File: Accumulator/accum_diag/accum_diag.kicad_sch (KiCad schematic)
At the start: 20 parts, among them K1 Contactor, K2 Contactor, K3 Precharge Relay, U2 Precharge

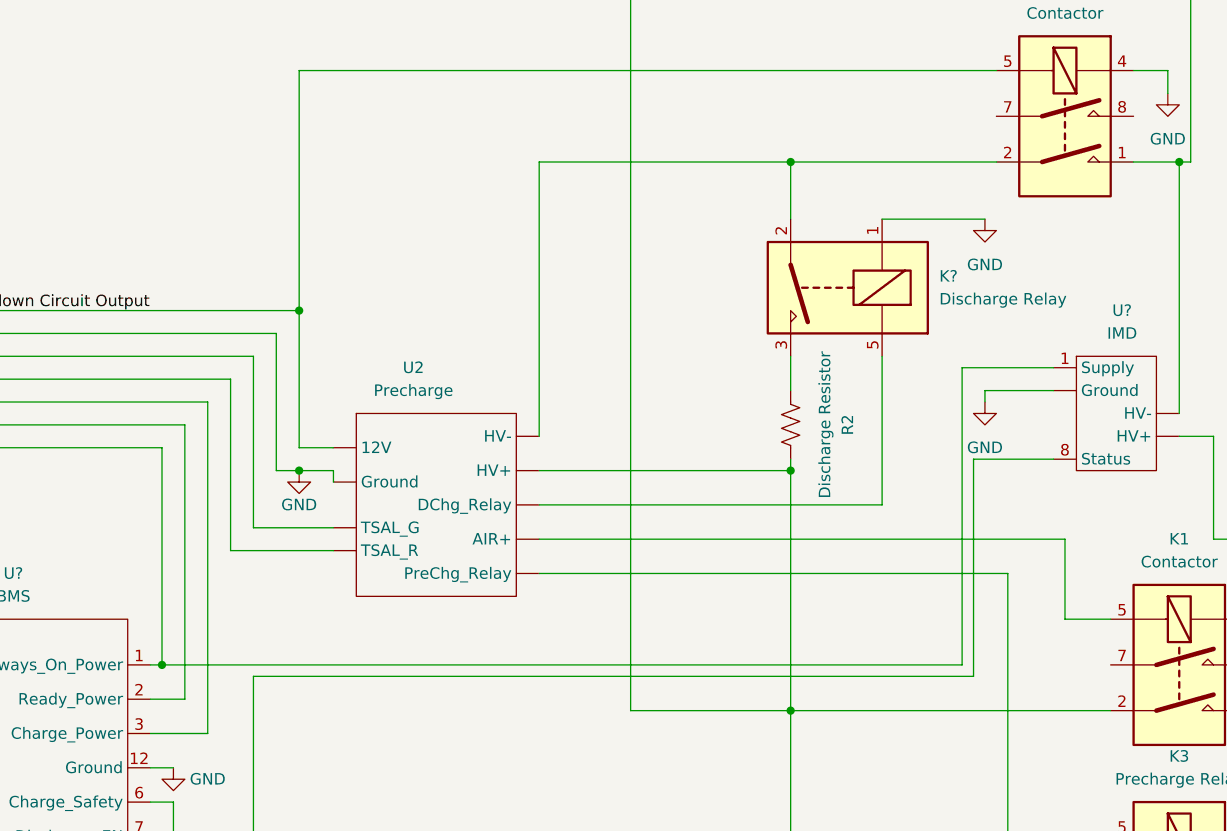
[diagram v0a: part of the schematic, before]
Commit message: Added GLV connection to precharge symbol
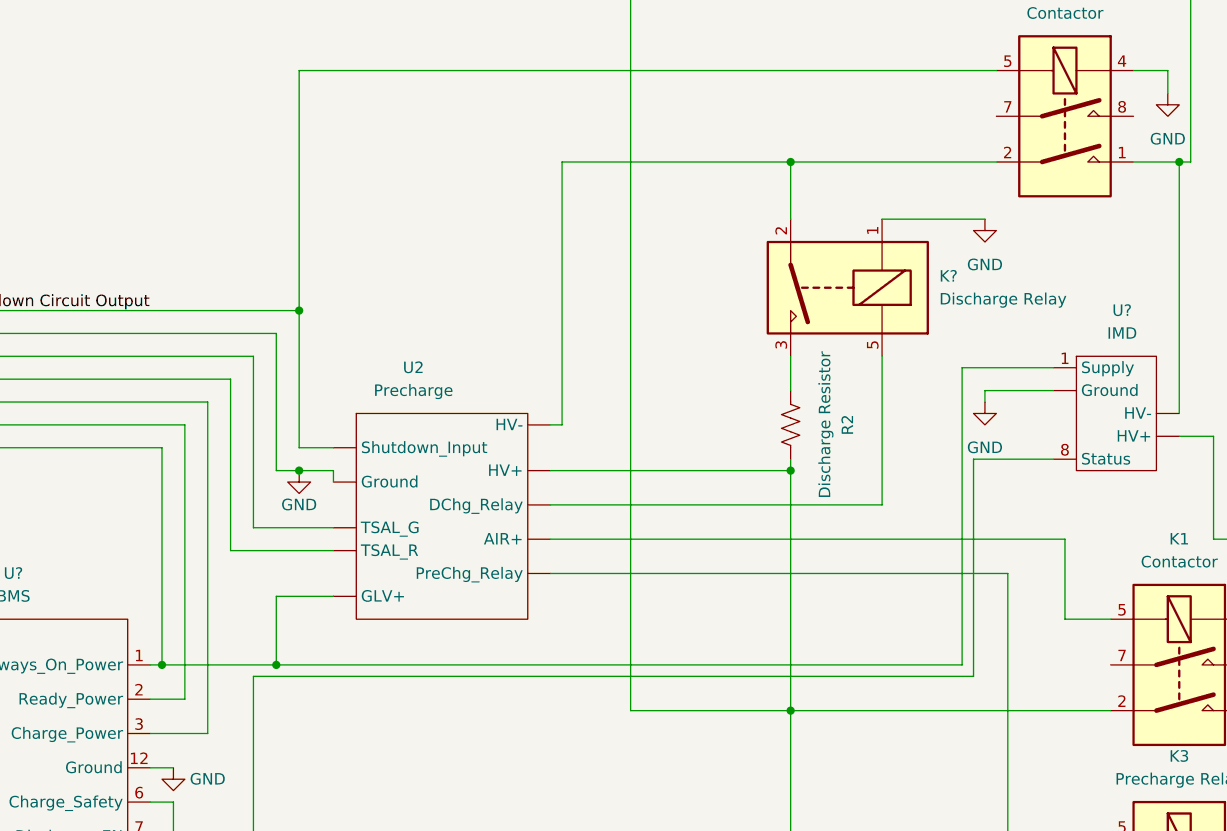
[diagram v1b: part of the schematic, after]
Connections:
- net Always on Power: now also U2. (TSAL_R)
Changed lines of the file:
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@@
   (junction (at 248.92 115.57) (diameter 0) (color 0 0 0 0)
   )
+  (junction (at 119.38 110.49) (diameter 0) (color 0 0 0 0)
+  )
+  (junction (at 189.23 54.61) (diameter 0) (color 0 0 0 0)
+  )
+  (junction (at 248.92 96.52) (diameter 0) (color 0 0 0 0)
+  )
+  (junction (at 189.23 115.57) (diameter 0) (color 0 0 0 0)
+  )
+  (junction (at 233.68 22.86) (diameter 0) (color 0 0 0 0)
+  )
+  (junction (at 134.62 71.12) (diameter 0) (color 0 0 0 0)
+  )
+  (junction (at 134.62 88.9) (diameter 0) (color 0 0 0 0)
+  )
+  (junction (at 232.41 54.61) (diameter 0) (color 0 0 0 0)
+  )
+  (junction (at 132.08 110.49) (diameter 0) (color 0 0 0 0)
+  )
   (junction (at 189.23 88.9) (diameter 0) (color 0 0 0 0)
   )
-  (junction (at 119.38 110.49) (diameter 0) (color 0 0 0 0)
-  )
-  (junction (at 189.23 54.61) (diameter 0) (color 0 0 0 0)
-  )
-  (junction (at 248.92 96.52) (diameter 0) (color 0 0 0 0)
-  )
-  (junction (at 189.23 115.57) (diameter 0) (color 0 0 0 0)
-  )
-  (junction (at 233.68 22.86) (diameter 0) (color 0 0 0 0)
-  )
-  (junction (at 134.62 71.12) (diameter 0) (color 0 0 0 0)
-  )
-  (junction (at 134.62 88.9) (diameter 0) (color 0 0 0 0)
-  )
-  (junction (at 232.41 54.61) (diameter 0) (color 0 0 0 0)
-  )
   (wire (pts (xy 129.54 111.76) (xy 129.54 140.97))
     (stroke (width 0) (type default) (color 0 0 0 0))
@@
     (stroke (width 0) (type default) (color 0 0 0 0))
   )
+  (wire (pts (xy 199.39 76.2) (xy 199.39 92.71))
+    (stroke (width 0) (type default) (color 0 0 0 0))
+  )
   (wire (pts (xy 45.72 104.14) (xy 60.96 104.14))
     (stroke (width 0) (type default) (color 0 0 0 0))
@@
     (stroke (width 0) (type default) (color 0 0 0 0))
   )
+  (wire (pts (xy 162.56 88.9) (xy 189.23 88.9))
+    (stroke (width 0) (type default) (color 0 0 0 0))
+  )
   (wire (pts (xy 46.99 30.48) (xy 227.33 30.48))
     (stroke (width 0) (type default) (color 0 0 0 0))
@@
     (stroke (width 0) (type default) (color 0 0 0 0))
   )
+  (wire (pts (xy 189.23 88.9) (xy 189.23 115.57))
+    (stroke (width 0) (type default) (color 0 0 0 0))
+  )
   (wire (pts (xy 210.82 80.01) (xy 210.82 81.28))
     (stroke (width 0) (type default) (color 0 0 0 0))
@@
     (stroke (width 0) (type default) (color 0 0 0 0))
   )
+  (wire (pts (xy 163.83 83.82) (xy 162.56 83.82))
+    (stroke (width 0) (type default) (color 0 0 0 0))
+  )
   (wire (pts (xy 46.99 38.1) (xy 46.99 66.04))
     (stroke (width 0) (type default) (color 0 0 0 0))
   )
-  (wire (pts (xy 161.29 54.61) (xy 189.23 54.61))
+  (wire (pts (xy 163.83 54.61) (xy 189.23 54.61))
     (stroke (width 0) (type default) (color 0 0 0 0))
   )
@@
     (stroke (width 0) (type default) (color 0 0 0 0))
   )
+  (wire (pts (xy 132.08 102.87) (xy 132.08 110.49))
+    (stroke (width 0) (type default) (color 0 0 0 0))
+  )
   (wire (pts (xy 213.36 100.33) (xy 213.36 129.54))
     (stroke (width 0) (type default) (color 0 0 0 0))
@@
     (stroke (width 0) (type default) (color 0 0 0 0))
   )
+  (wire (pts (xy 199.39 92.71) (xy 162.56 92.71))
+    (stroke (width 0) (type default) (color 0 0 0 0))
+  )
   (wire (pts (xy 248.92 81.28) (xy 248.92 82.55))
     (stroke (width 0) (type default) (color 0 0 0 0))
   )
-  (wire (pts (xy 199.39 76.2) (xy 199.39 92.71))
-    (stroke (width 0) (type default) (color 0 0 0 0))
-  )
   (wire (pts (xy 257.81 64.77) (xy 248.92 64.77))
     (stroke (width 0) (type default) (color 0 0 0 0))
@@
     (stroke (width 0) (type default) (color 0 0 0 0))
   )
-  (wire (pts (xy 161.29 88.9) (xy 189.23 88.9))
-    (stroke (width 0) (type default) (color 0 0 0 0))
-  )
   (wire (pts (xy 124.46 81.28) (xy 45.72 81.28))
     (stroke (width 0) (type default) (color 0 0 0 0))
@@
     (stroke (width 0) (type default) (color 0 0 0 0))
   )
-  (wire (pts (xy 213.36 100.33) (xy 161.29 100.33))
-    (stroke (width 0) (type default) (color 0 0 0 0))
-  )
   (wire (pts (xy 227.33 30.48) (xy 227.33 22.86))
     (stroke (width 0) (type default) (color 0 0 0 0))
@@
     (stroke (width 0) (type default) (color 0 0 0 0))
   )
+  (wire (pts (xy 162.56 100.33) (xy 213.36 100.33))
+    (stroke (width 0) (type default) (color 0 0 0 0))
+  )
   (wire (pts (xy 132.08 88.9) (xy 132.08 73.66))
     (stroke (width 0) (type default) (color 0 0 0 0))
@@
     (stroke (width 0) (type default) (color 0 0 0 0))
   )
+  (wire (pts (xy 138.43 102.87) (xy 132.08 102.87))
+    (stroke (width 0) (type default) (color 0 0 0 0))
+  )
   (wire (pts (xy 248.92 62.23) (xy 257.81 62.23))
     (stroke (width 0) (type default) (color 0 0 0 0))
@@
     (stroke (width 0) (type default) (color 0 0 0 0))
   )
+  (wire (pts (xy 132.08 110.49) (xy 208.28 110.49))
+    (stroke (width 0) (type default) (color 0 0 0 0))
+  )
   (wire (pts (xy 120.65 125.73) (xy 120.65 138.43))
     (stroke (width 0) (type default) (color 0 0 0 0))
@@
     (stroke (width 0) (type default) (color 0 0 0 0))
   )
-  (wire (pts (xy 161.29 85.09) (xy 161.29 54.61))
-    (stroke (width 0) (type default) (color 0 0 0 0))
-  )
   (wire (pts (xy 86.36 127) (xy 63.5 127))
     (stroke (width 0) (type default) (color 0 0 0 0))
@@
     (stroke (width 0) (type default) (color 0 0 0 0))
   )
-  (wire (pts (xy 161.29 96.52) (xy 219.71 96.52))
-    (stroke (width 0) (type default) (color 0 0 0 0))
-  )
   (wire (pts (xy 209.55 111.76) (xy 129.54 111.76))
     (stroke (width 0) (type default) (color 0 0 0 0))
@@
     (stroke (width 0) (type default) (color 0 0 0 0))
   )
+  (wire (pts (xy 163.83 54.61) (xy 163.83 83.82))
+    (stroke (width 0) (type default) (color 0 0 0 0))
+  )
+  (wire (pts (xy 219.71 96.52) (xy 219.71 105.41))
+    (stroke (width 0) (type default) (color 0 0 0 0))
+  )
   (wire (pts (xy 63.5 127) (xy 63.5 101.6))
     (stroke (width 0) (type default) (color 0 0 0 0))
@@
     (stroke (width 0) (type default) (color 0 0 0 0))
   )
-  (wire (pts (xy 219.71 96.52) (xy 219.71 105.41))
-    (stroke (width 0) (type default) (color 0 0 0 0))
-  )
   (wire (pts (xy 71.12 93.98) (xy 45.72 93.98))
     (stroke (width 0) (type default) (color 0 0 0 0))
   )
+  (wire (pts (xy 162.56 96.52) (xy 219.71 96.52))
+    (stroke (width 0) (type default) (color 0 0 0 0))
+  )
   (wire (pts (xy 119.38 110.49) (xy 119.38 86.36))
     (stroke (width 0) (type default) (color 0 0 0 0))
   )
-  (wire (pts (xy 161.29 92.71) (xy 199.39 92.71))
-    (stroke (width 0) (type default) (color 0 0 0 0))
-  )
   (wire (pts (xy 124.46 118.11) (xy 124.46 81.28))
     (stroke (width 0) (type default) (color 0 0 0 0))
   )
-  (wire (pts (xy 189.23 88.9) (xy 189.23 115.57))
-    (stroke (width 0) (type default) (color 0 0 0 0))
-  )
-  (wire (pts (xy 119.38 110.49) (xy 208.28 110.49))
+  (wire (pts (xy 119.38 110.49) (xy 132.08 110.49))
     (stroke (width 0) (type default) (color 0 0 0 0))
   )
@@
     (pin "")
     (pin "")
+    (pin "")
